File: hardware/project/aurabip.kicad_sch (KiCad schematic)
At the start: 50 parts, among them J1 USB-C, J2 AKKU LiPo, J3 LAUTSPRECHER 8R 1W, J4 OLED WS 1.32 SPI, J5 u.FL 868, SW1 EIN/AUS, SW2 RESET, SW3 BOOT/USER, U1 ESP32-S3-MINI-1-N8, U10 E22-900M22S, U2 BMP581, U3 LSM6DSO32, U4 SHT40-AD1B, U5 Quectel L96, U6 MAX98357A, U7 MCP73831-2, U8 ME6217C33M5G, U9 USBLC6-2SC6

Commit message: fix(hardware): alle kritischen Pinouts gegen Datenblaetter verifiziert
Web-Recherche gegen Originalquellen (Ebyte Manual v1.3, Quectel HW
Design V1.4, ADI Rev 7, ST Rev 1) — drei von vier Annahmen waren falsch:
- E22-900M22S: 14x20/Pitch 1.27 statt 16x26/2.2, Pin-Map komplett neu
- L96: LCC-31 statt 12 Pads; RF-Bruecke R12 (RF_OUT->RF_IN, sonst kein
  GPS!), RXD-Pegelteiler R13/R14 (VIHmax 3.1V), C16, Antennen-Keepout
- MAX98357A: TQFN-Pinout neu (Pin 8 war VDD, nicht GND!), EP1.23-Footprint
- LSM6DSO32: Pinout bestaetigt, ST-Footprint statt Bosch (0.1mm-Versatz)

Dazu: Gehaeuse-Generator fuer Fusion 360 (hardware/fusion/, Varianten
audio/vision, Akku 504050, K-28-WP-Sitz, Antennen-Nische, Display-
Fenster), Board-STEP-Export, PCBWay-Fertigungspaket (export_fab.ps1 +
BOM-Generator), Akku auf 504050 1500mAh.

Co-Authored-By: Claude Fable 5 <noreply@anthropic.com>
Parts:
- added C16: 10u, Capacitor_SMD:C_0603_1608Metric, symbol Device:C
- added R12: 0R, Resistor_SMD:R_0402_1005Metric, symbol Device:R
- added R13: 1k, Resistor_SMD:R_0402_1005Metric, symbol Device:R
- added R14: 2k, Resistor_SMD:R_0402_1005Metric, symbol Device:R
- U3: footprint Package_LGA:Bosch_LGA-14_3x2.5mm_P0.5mm -> Package_LGA:LGA-14_3x2.5mm_P0.5mm_LayoutBorder3x4y
- U6: footprint Package_DFN_QFN:QFN-16-1EP_3x3mm_P0.5mm_EP1.75x1.75mm -> Package_DFN_QFN:TQFN-16-1EP_3x3mm_P0.5mm_EP1.23x1.23mm
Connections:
- net +3V3: now also U10.9 (VCC), U5.9 (VCC), C16.1; no longer U10.11 (VCC), U5.6 (V_BCKP)
- net AMP_SD: now also U6.4 (SD_MODE); no longer U6.5 (SD_MODE)
- net GND: now also U10.10 (GND6), U10.11 (GND7), U10.22 (GND10), U10.3 (GND3), U10.4 (GND4), U10.5 (GND5), U5.10 (GND3), U5.11 (GND4), U5.13 (GND6), U5.14 (GND7), U5.15 (GND8), U5.18 (GND9), U5.19 (GND10), U5.21 (GND11), U5.22 (GND12), U5.27 (GND13), U5.31 (GND14), U5.4 (GND), U5.5 (GND2), U6.11 (GND2), U6.15 (GND3), U6.3 (GND), C16.2, R14.2; no longer U5.1 (GND), U5.3 (GND2), U5.7 (GND3), U6.8 (GND)
- net GNSS_RXD: now also R13.1; no longer U5.10 (RXD)
- net GNSS_TXD: now also U5.25 (TXD1); no longer U5.9 (TXD)
- net I2S_BCLK: now also U6.16 (BCLK); no longer U6.2 (BCLK)
- net I2S_DOUT: now also U6.1 (DIN); no longer U6.3 (DIN)
- net I2S_LRCK: now also U6.14 (LRCLK); no longer U6.1 (LRCLK)
- net LORA_ANT: now also U10.21 (ANT); no longer U10.3 (ANT)
- net LORA_BUSY: now also U10.14 (BUSY); no longer U10.15 (BUSY)
- net LORA_DIO1: now also U10.13 (DIO1); no longer U10.14 (DIO1)
- net LORA_RST: now also U10.15 (NRST); no longer U10.10 (NRST)
- net LORA_RXEN: now also U10.6 (RXEN); no longer U10.7 (RXEN)
- net LORA_TXEN: now also U10.7 (TXEN); no longer U10.6 (TXEN)
- net SPK_N: now also U6.10 (OUTN); no longer U6.11 (OUTN)
- net VBAT: now also U6.7 (VDD), U6.8 (VDD2); no longer U6.13 (VDD)
- new net GNSS_RXD_DIV: R13.2, R14.1, U5.26 (RXD1)
- new net L96_RFIN: R12.2, U5.17 (RF_IN)
- new net L96_RFOUT: R12.1, U5.16 (RF_OUT)
- no-connect marks 24 -> 32

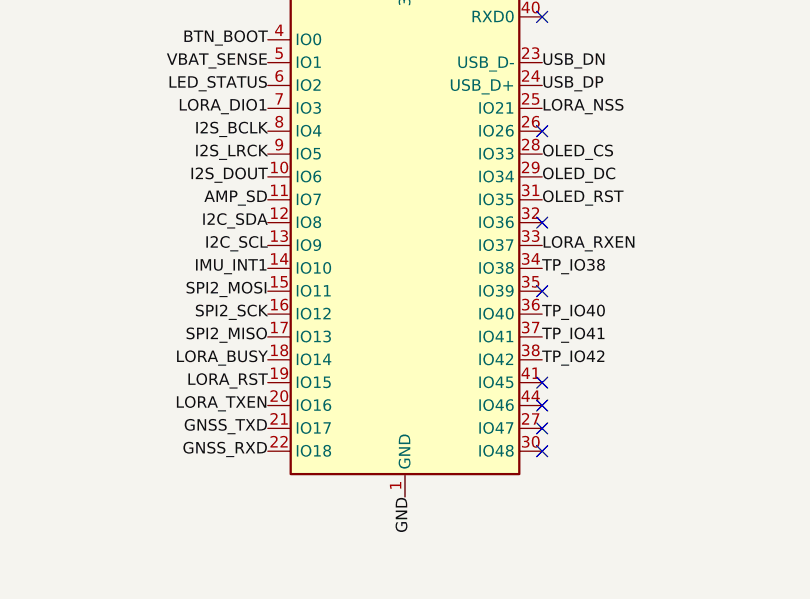
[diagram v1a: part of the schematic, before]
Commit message: feat(route): Platine FERTIG — DRC 0 Verstoesse, 0 unverbunden
Eigener A*-Maze-Router (maze_router.py): 0.1-mm-Raster, 2 Lagen,
Via-Uebergaenge, exaktes Hindernismodell (Pads/Tracks/Vias/Moat/
Keepouts/NPTH), --narrow (5 mil), --ortho (keine Eckenschnitte),
--rip (Rip-up&Reroute), --pairs, Via-in-Pad-Rettung mit praeziser
Geometriepruefung, systematische Insel-Heilung (Waisen-Pours).

Bugs auf dem Weg: A*-f/g-Verwechslung, SWIG-__eq__, Diagonal-
Eckenschnitte, Splice-Diagonalen. I2S_DOUT per GPIO-Matrix auf
IO47 verlegt (IO6-Region war zugebaut) — Schema/Firmware-Doku folgt.

Fertigungspaket: Gerber-ZIP, Bohrdaten, Pick&Place beidseitig,
STEP-Modell. VOR BESTELLUNG: BOM-CSV neu generieren (Datei war
gesperrt) + T-H1 Teileverfuegbarkeit.

Co-Authored-By: Claude Fable 5 <noreply@anthropic.com>
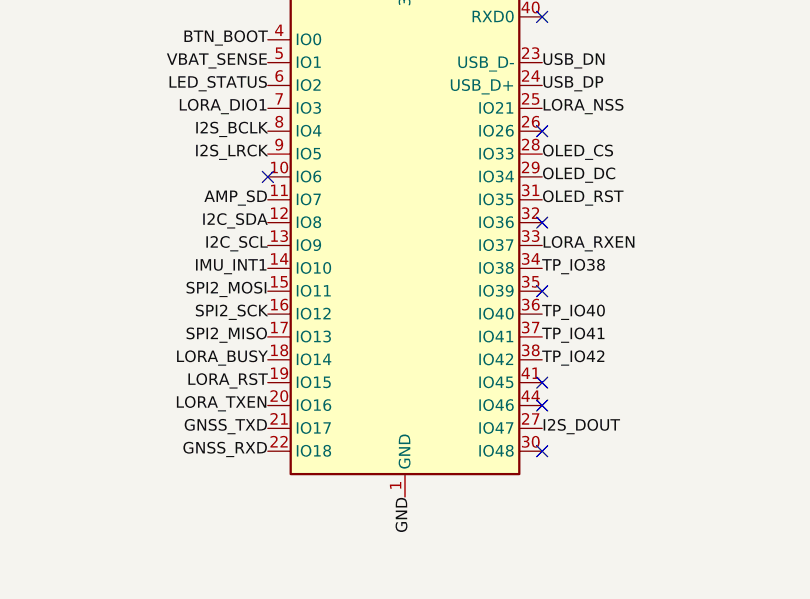
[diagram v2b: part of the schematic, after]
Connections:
- net I2S_DOUT: now also U1.27 (IO47); no longer U1.10 (IO6)

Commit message: feat(emv): Review umgesetzt — Board-RF eliminiert, SPK-Paar enger
EMV-Review (Ivo) Punkt 3 nicht repariert sondern eliminiert: die
34-mm-ANT-Leitung (lag nach Modul-Flip quer ueber halbes Board, 15
Nachbarsignale) faellt weg — Flexantenne steckt DIREKT auf die
IPX-Buchse des E22-Moduls. J5 + LORA_ANT komplett entfernt
(Schema ERC 0, Board DRC 0/0). SPK_P neu als Ortho-Route neben
SPK_N (Schleifenflaeche runter). Audit bestaetigt: Innenlagen
tragen NULL Signale — GND/3V3-Planes durchgehend.

Co-Authored-By: Claude Fable 5 <noreply@anthropic.com>
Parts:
- removed J5: u.FL 868, Connector_Coaxial:U.FL_Hirose_U.FL-R-SMT-1_Vertical, symbol Connector:Conn_Coaxial
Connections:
- net LORA_ANT: no longer names the net of U10.21 (ANT)
- no-connect marks 32 -> 33
